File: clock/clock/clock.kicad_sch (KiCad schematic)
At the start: 44 parts, among them J1 AVR-ISP-6, J10 Conn_01x07_Male, J11 CV_IN, J12 CLOCK_OUT, J13 SUBDIV_OUT, J2 EURORACK_CONN_10, J3 Conn_01x05_Female, J4 Conn_01x05_Male, J5 Conn_01x05_Female, J6 Conn_01x05_Male, J7 Conn_01x05_Female, J8 Conn_01x05_Male, J9 Conn_01x07_Female, SW1 SW_Push, SW2 SW_Push, SW3 Rotary_Encoder_Switch, U1 ATmega328P-PU, U2 L7805, U3 SM460281N, U4 SM460281N, U5 SM460281N, Y1 16MHz

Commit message: re-annotate schematic
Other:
- note added: "7-segment display"
- note added: "IO jacks"
- note added: "controls"
- note added: "mcu and programming pins"
- note added: "power supply"
- company: (none) -> rabid.audio
- title: (none) -> CLK
- moved on the sheet: C1, C2, C3, C4, C5, C6, D1, D2, D3, J1, J10, J11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

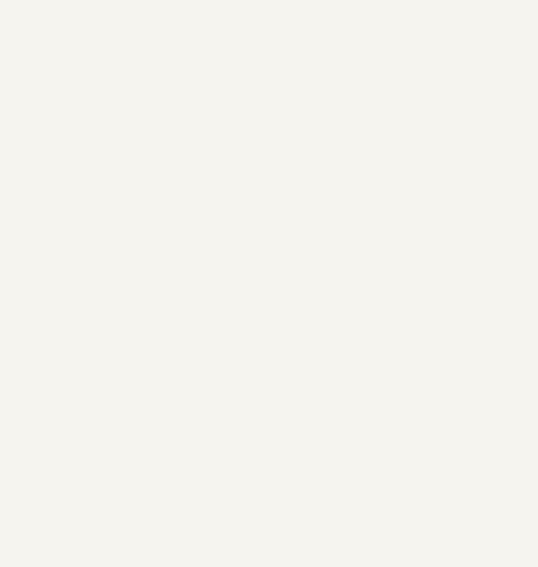
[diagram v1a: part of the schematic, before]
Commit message: fix some PCB bugs
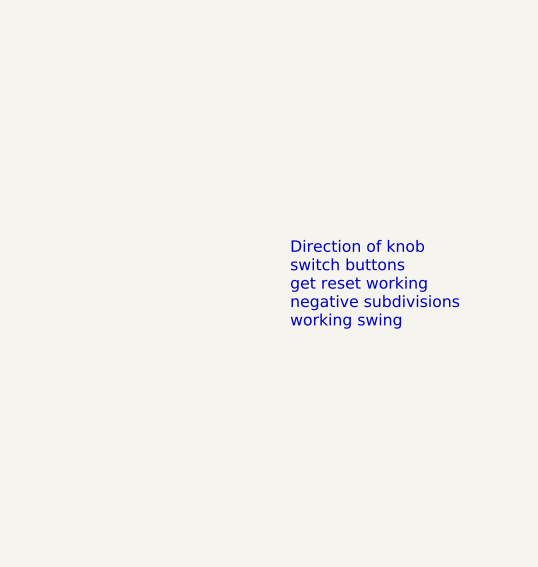
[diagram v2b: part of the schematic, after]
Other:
- note added: "Direction of knob switch buttons get reset working negative subdivisions working swing"
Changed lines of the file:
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@@
+    (effects (font (size 1.27 1.27)) (justify left bottom))
+  )
+  (text "Direction of knob\nswitch buttons\nget reset working\nnegative subdivisions\nworking swing"
+    (at 368.3 83.185 0)
     (effects (font (size 1.27 1.27)) (justify left bottom))
   )

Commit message: fix inputs
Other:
- note removed: "Direction of knob switch buttons get reset working negative subdivisions working swing"
- moved on the sheet: D3, J11, J12, J13, R14, R15

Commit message: pause support
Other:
- note added: "screw with spacer to panel at bottom bigger clock footprint move regulator so more space for programmer"
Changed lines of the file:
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@@
+    (effects (font (size 1.27 1.27)) (justify left bottom))
+  )
+  (text "screw with spacer to panel at bottom\nbigger clock footprint\nmove regulator so more space for programmer\n"
+    (at 220.98 175.26 0)
     (effects (font (size 1.27 1.27)) (justify left bottom))
   )

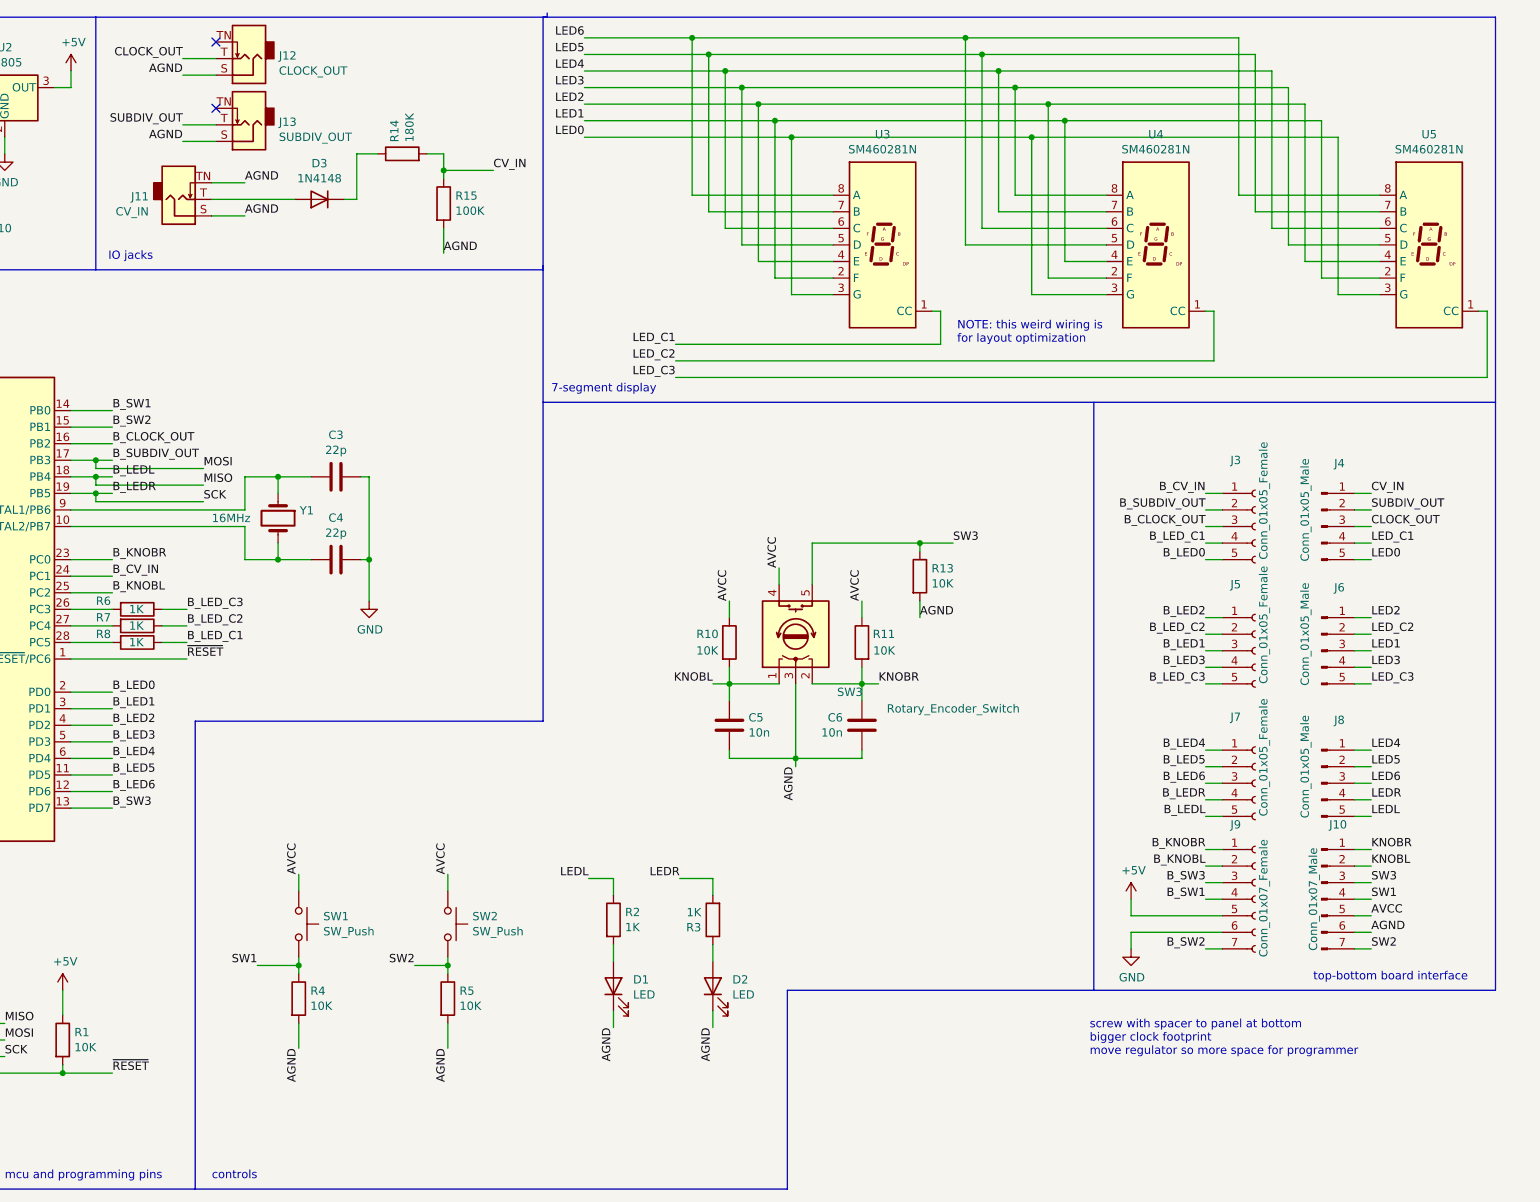
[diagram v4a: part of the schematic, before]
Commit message: make ground plane connected, move LEDs wide
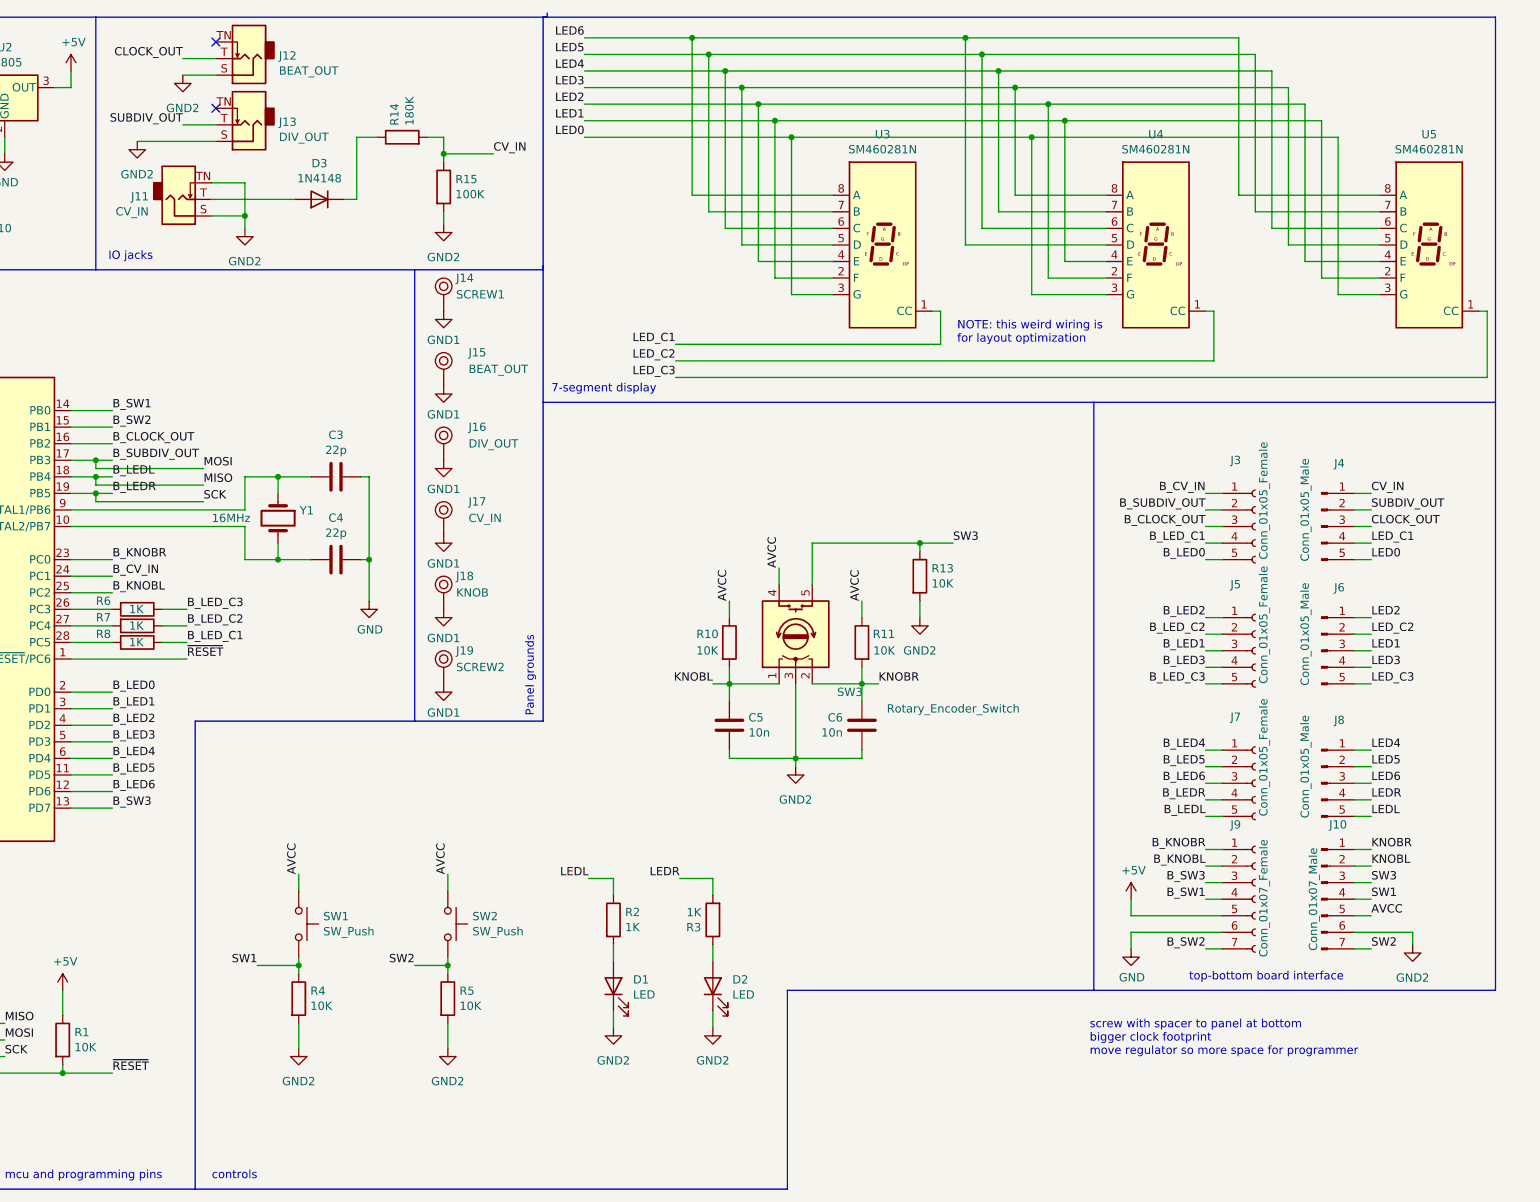
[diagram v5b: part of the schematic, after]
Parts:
- added J14: SCREW1, synth:eurorack_screw_hole, symbol synth:PanelItem
- added J15: BEAT_OUT, synth:thonkiconn_hole, symbol synth:PanelItem
- added J16: DIV_OUT, synth:thonkiconn_hole, symbol synth:PanelItem
- added J17: CV_IN, synth:thonkiconn_hole, symbol synth:PanelItem
- added J18: KNOB, synth:knob_hole, symbol synth:PanelItem
- added J19: SCREW2, synth:eurorack_screw_hole, symbol synth:PanelItem
- J12: value CLOCK_OUT -> BEAT_OUT
- J13: value SUBDIV_OUT -> DIV_OUT
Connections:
- net AGND renamed GND2
- new net GND1: J14.1, J15.1, J16.1, J17.1, J18.1, J19.1
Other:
- note added: "Panel grounds"
- moved on the sheet: R14, R15

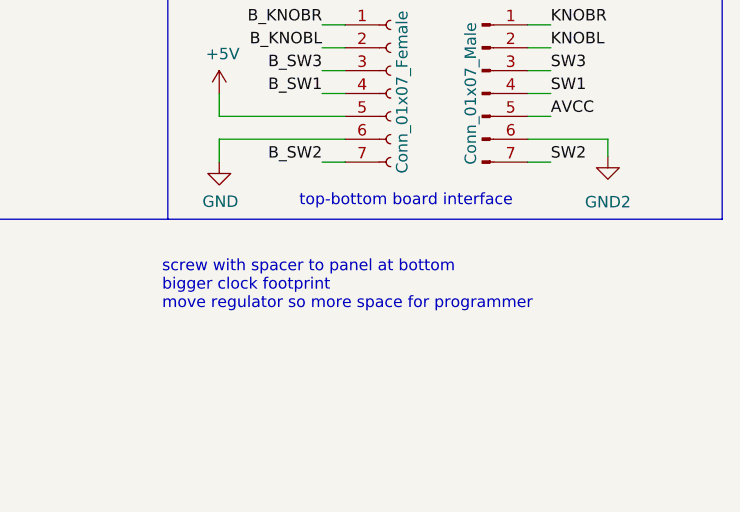
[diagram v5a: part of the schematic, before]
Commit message: increase crystal footprint
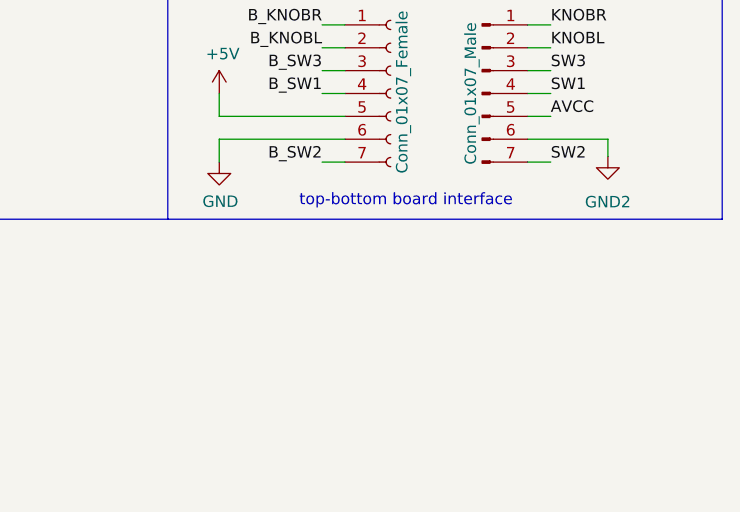
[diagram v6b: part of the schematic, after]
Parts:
- Y1: footprint Crystal:Crystal_HC52-8mm_Vertical -> kicad-official/Crystal.pretty:Crystal_HC50_Vertical
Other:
- note removed: "screw with spacer to panel at bottom bigger clock footprint move regulator so more space for programmer"
- title: CLK -> The Count
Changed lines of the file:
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@@
   (paper "A4")
   (title_block
-    (title "CLK")
-    (date "2023-01-01")
-    (rev "A")
+    (title "The Count")
+    (date "2023-04-30")
+    (rev "B")
     (company "rabid.audio")
   )
@@
     (effects (font (size 1.27 1.27)) (justify left bottom))
   )
-  (text "screw with spacer to panel at bottom\nbigger clock footprint\nmove regulator so more space for programmer\n"
-    (at 220.98 175.26 0)
-    (effects (font (size 1.27 1.27)) (justify left bottom))
-  )
   (text "mcu and programming pins" (at 54.61 194.31 0)
     (effects (font (size 1.27 1.27)) (justify left bottom))
@@
       (effects (font (size 1.27 1.27)) (justify left))
     )
-    (property "Footprint" "Crystal:Crystal_HC52-8mm_Vertical" (id 2) (at 96.52 92.71 0)
+    (property "Footprint" "kicad-official/Crystal.pretty:Crystal_HC50_Vertical" (id 2) (at 96.52 92.71 0)
       (effects (font (size 1.27 1.27)) hide)
     )
@@
     )
     (path "/00000000-0000-0000-0000-0000631d1d82"
-      (reference "Y1") (unit 1) (value "16MHz") (footprint "Crystal:Crystal_HC52-8mm_Vertical")
-    )
-  )
+      (reference "Y1") (unit 1) (value "16MHz") (footprint "kicad-official/Crystal.pretty:Crystal_HC50_Vertical")
+    )
+  )
